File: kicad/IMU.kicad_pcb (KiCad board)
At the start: 4 copper layers, 30 x 30 mm, 78 parts, among them IC1 FT232RQ, P1 M1P, P10 CONN_01X02, P11 CONN_02X05, P2 M1N, P3 M3P, P4 M3N, P5 JTAG_DB, P6 M2P, P7 M2N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

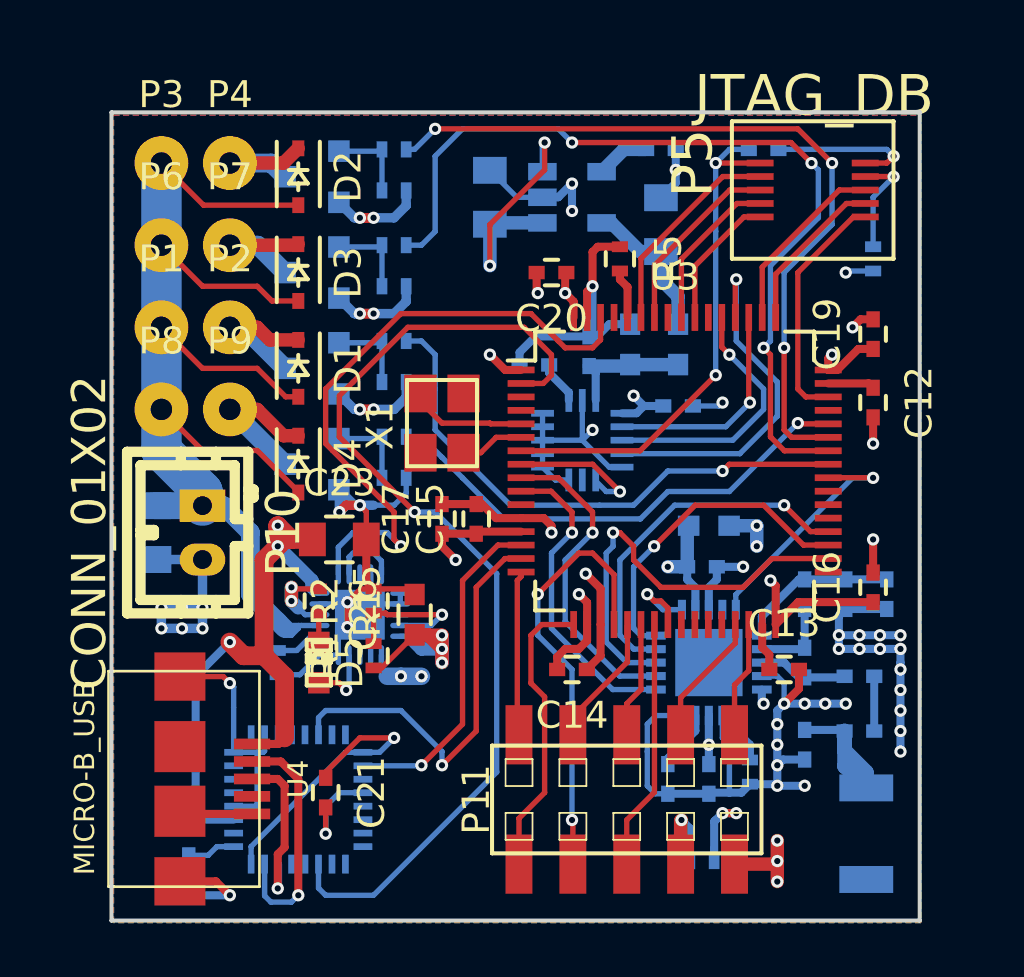
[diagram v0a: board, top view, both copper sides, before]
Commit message: Added edge pads and some more vias.
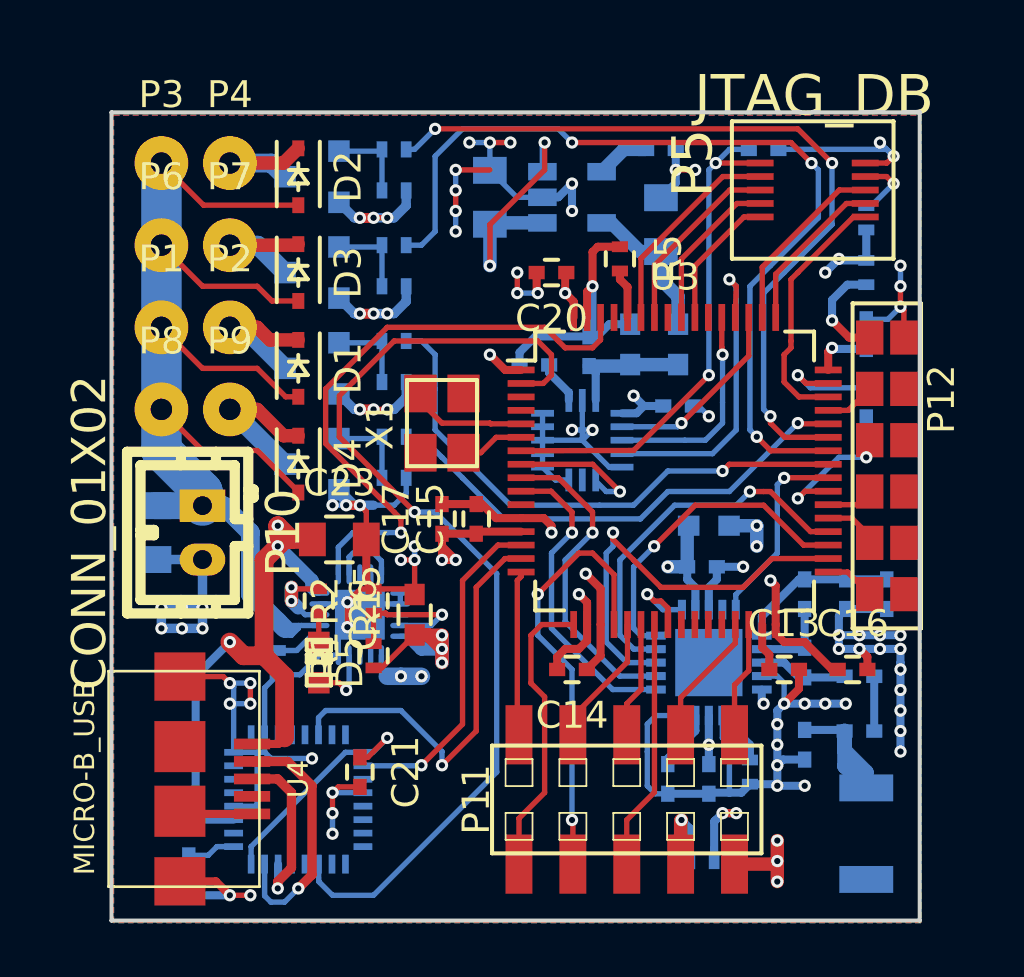
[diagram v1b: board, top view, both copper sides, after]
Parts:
- added P12: CONN_02X06, Connect:GS_6x2, F.Cu at (128.8, 82.8)
- added R17: 100, Resistors_SMD:R_0402, B.Cu at (128.0, 75.9)
- C12, C19: moved to B.Cu
- moved C16 3.14 mm to (127.5, 90.7), turned to 0 degrees
- moved R14 1.55 mm to (128.0, 73.9)
- moved C21 1.48 mm to (109.2, 94.5)
- moved C12 0.25 mm to (128.0, 80.8)
- moved C19 0.25 mm to (128.0, 78.2)
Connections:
- P11 pad 9: GND -> Net-(P11-Pad9)
- U3 pad 33: Net-(U3-Pad33) -> /Microcontroller/PAD5
- U3 pad 37: Net-(U3-Pad37) -> /Microcontroller/PAD4
- U3 pad 38: Net-(U3-Pad38) -> /Microcontroller/PAD3
- U3 pad 39: Net-(U3-Pad39) -> /Microcontroller/PAD2
- U3 pad 45: Net-(U3-Pad45) -> /Microcontroller/PAD1
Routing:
- net GND: track 152.8 -> 171.1 mm, vias 58 -> 81
- net /Microcontroller/PAD2: track 0.00 -> 5.10 mm, vias 0 -> 2
- net Net-(P12-Pad1): track 0.00 -> 3.93 mm, vias 0 -> 1
- net Net-(P11-Pad9): track 0.00 -> 3.16 mm, vias 0 -> 3
- net Net-(C12-Pad1): track 1.73 -> 3.99 mm, vias 0 -> 1
- net Net-(C21-Pad1): track 10.9 -> 8.69 mm
- net VDD: track 35.7 -> 37.9 mm, vias 15 -> 17
- net /Microcontroller/PAD4: track 0.00 -> 2.07 mm
- net /Microcontroller/PAD5: track 0.00 -> 1.88 mm
- net /Microcontroller/PAD1: track 0.00 -> 1.87 mm
- net /Mems and Radio/MEMS_MOSI: track 9.79 -> 7.92 mm
- net /Mems and Radio/NRF24_OSC: track 9.12 -> 7.28 mm
- net /Microcontroller/PAD3: track 0.00 -> 1.74 mm
- net /Mems and Radio/MEMS_MISO: track 13.5 -> 11.8 mm
- net Net-(P5-Pad4): track 3.97 -> 2.52 mm
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
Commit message: Added status LEDs to FTDI IC and bat voltage to mcu ADC.
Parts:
- added D6: TXLED, LEDs:LED-0603, B.Cu at (103.1, 91.2)
- added D7: RXLED, LEDs:LED-0603, B.Cu at (101.9, 91.2)
- added R18: 100k, Resistors_SMD:R_0402, F.Cu at (110.0, 75.9)
- added R19: 100k, Resistors_SMD:R_0402, F.Cu at (112.0, 75.9)
- added R20: 2k2, Resistors_SMD:R_0402, B.Cu at (102.4, 93.5)
- added R21: 2k2, Resistors_SMD:R_0402, B.Cu at (102.4, 95.0)
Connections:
- P11 pad 9: Net-(P11-Pad9) -> GND
- U3 pad 11: Net-(U3-Pad11) -> /Microcontroller/VBAT
- U3 pad 3: Net-(U3-Pad3) -> /Microcontroller/VBAT0
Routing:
- net /Microcontroller/VBAT: track 0.00 -> 11.6 mm, vias 0 -> 2
- net /Microcontroller/VBAT0: track 0.00 -> 6.97 mm, vias 0 -> 2
- net +5V: track 25.3 -> 29.3 mm
- net Net-(D7-Pad2): track 0.00 -> 3.69 mm
- net (no net): track 0.00 -> 3.56 mm, vias 0 -> 4
- net Net-(P11-Pad9): track 3.16 -> 0.00 mm, vias 3 -> 0
- net +BATT: track 49.4 -> 52.4 mm
- net Net-(IC1-Pad22): track 0.00 -> 2.70 mm
- net Net-(D6-Pad2): track 0.00 -> 2.34 mm
- net Net-(IC1-Pad21): track 0.00 -> 1.83 mm
- net GND: track 171.1 -> 170.7 mm, vias 81 -> 80

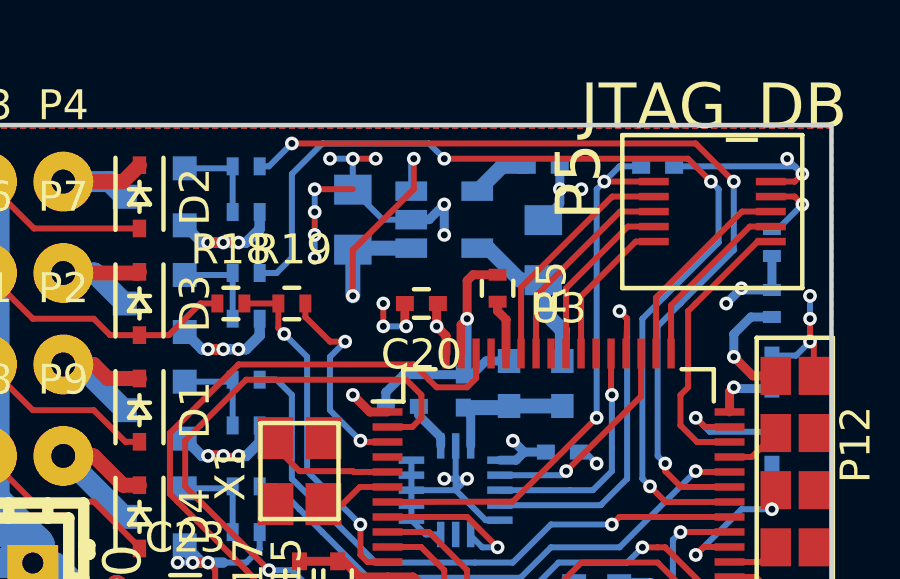
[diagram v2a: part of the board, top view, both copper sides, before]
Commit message: Changed LP2992 to TLV700 with better PSRR.
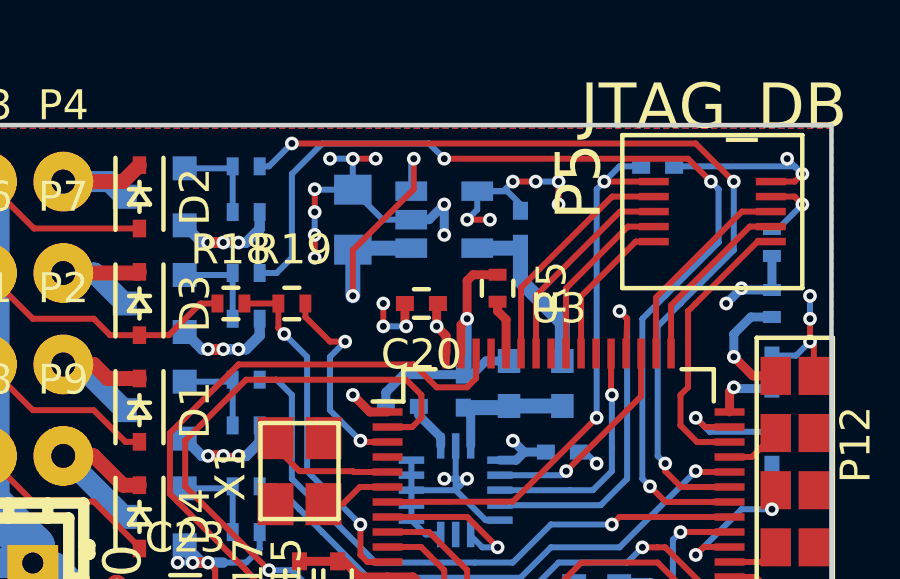
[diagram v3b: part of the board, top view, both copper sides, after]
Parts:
- removed C28: 10u, Capacitors_SMD:C_0805
- C27: value 10n -> 1u
- U6: value LP2992 -> TLV70033
- moved C27 2.17 mm to (119.6, 73.4), turned to 90 degrees
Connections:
- C27 pad 1: Net-(C27-Pad1) -> VAA
- U6 pad 4: Net-(C27-Pad1) -> GND
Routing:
- net GND: track 170.7 -> 178.8 mm, vias 80 -> 88
- net (no net): track 3.56 -> 0.00 mm, vias 4 -> 0
- net Net-(C27-Pad1): track 1.99 -> 0.00 mm
